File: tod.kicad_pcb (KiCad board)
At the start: 2 copper layers, 72 x 57 mm, 67 parts, among them J1 Conn_01x04, J2 Conn_01x03, J3 Conn_01x04, J4 Conn_01x03, Q1 BC856B, Q2 BC817, Q3 BC856B, Q4 BC817, Q5 BC856, Q6 BC817, Q7 BC856, Q8 BC817, U1 PC817, U2 PC817, U3 PC817, U4 PC817

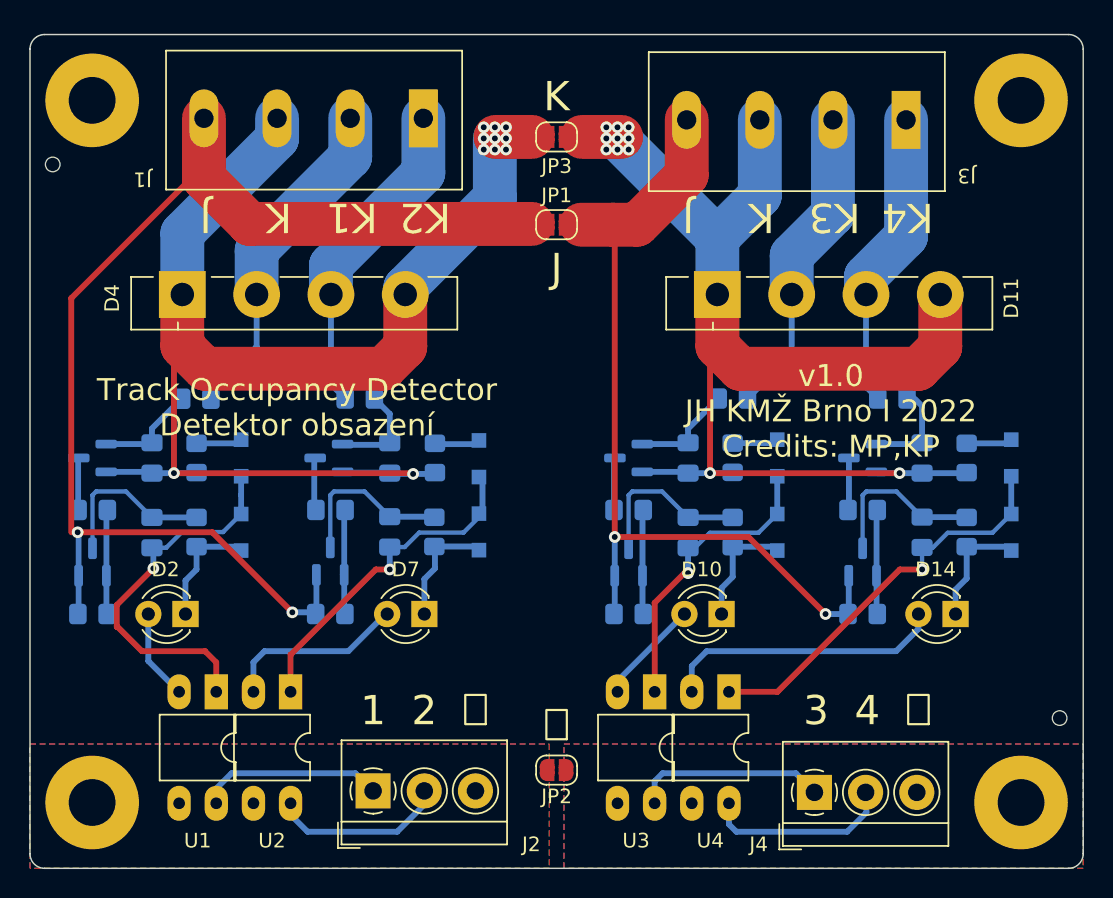
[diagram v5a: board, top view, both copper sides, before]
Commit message: Resolve DRC issues.
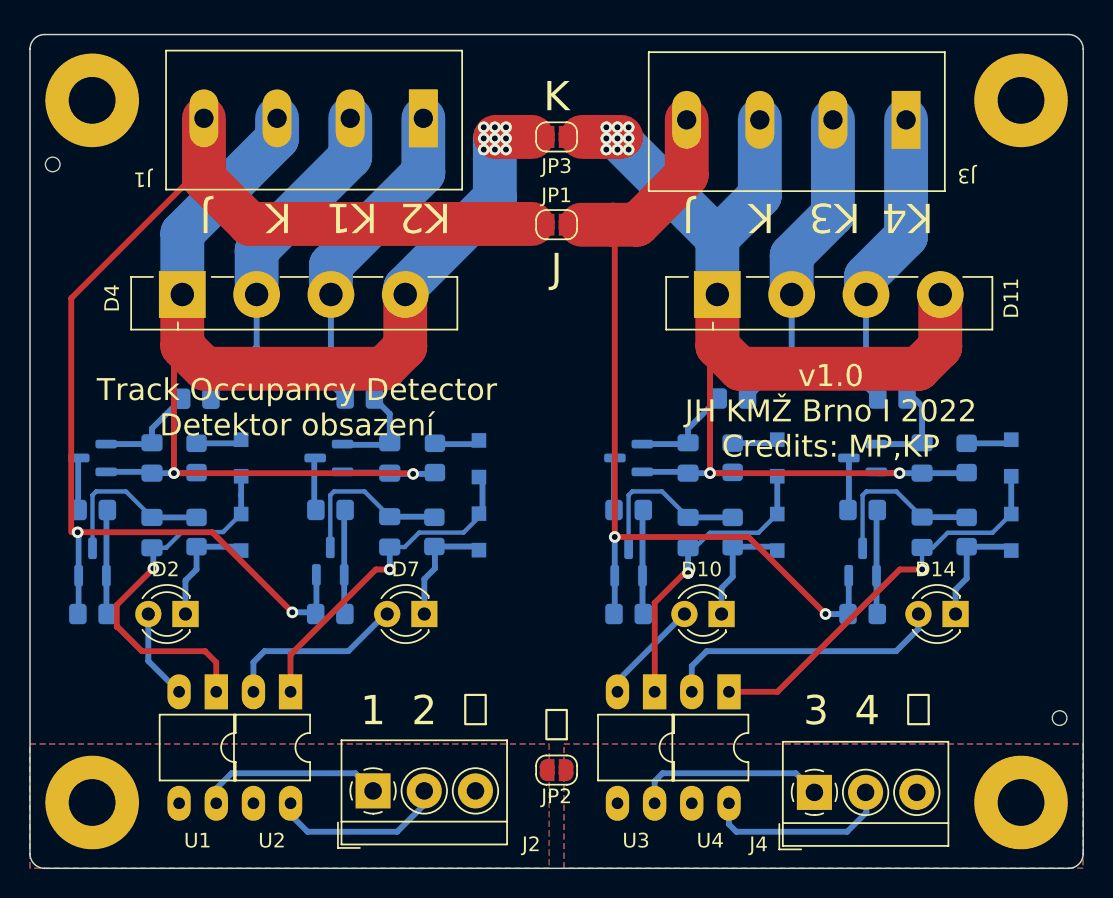
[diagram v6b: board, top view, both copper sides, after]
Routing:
- net /K1: track 93.5 -> 92.0 mm
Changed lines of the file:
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@@
   (segment (start 122.8405 92.9855) (end 122.862 92.964) (width 0.4) (layer "F.Cu") (net 1))
   (segment (start 138.654 84.358) (end 137.16 85.852) (width 3) (layer "F.Cu") (net 1))
-  (segment (start 122.936 81.25) (end 123.414 80.772) (width 0.4) (layer "F.Cu") (net 1))
   (segment (start 124.968 85.852) (end 123.414 84.298) (width 3) (layer "F.Cu") (net 1))
   (segment (start 122.8405 92.9855) (end 139.1395 92.9855) (width 0.4) (layer "F.Cu") (net 1))
-  (segment (start 122.8405 81.3455) (end 123.414 80.772) (width 0.4) (layer "F.Cu") (net 1))
   (segment (start 144.82 70) (end 147.32 70) (width 3) (layer "F.Cu") (net 1))
   (segment (start 122.8405 84.8715) (end 123.414 84.298) (width 0.4) (layer "F.Cu") (net 1))
@@
   (segment (start 137.434 95.9625) (end 140.6465 95.9625) (width 0.4) (layer "B.Cu") (net 7))
   (segment (start 133.53 98.0625) (end 133.53 94.488) (width 0.3) (layer "B.Cu") (net 7))
-  (segment (start 140.6465 95.9625) (end 140.684 96) (width 0.4) (layer "B.Cu") (net 7))
   (segment (start 175.23 80.772) (end 175.23 84.358) (width 3) (layer "F.Cu") (net 8))
   (segment (start 175.23 84.358) (end 173.736 85.852) (width 3) (layer "F.Cu") (net 8))
@@
   (segment (start 173.985 92.9855) (end 176.9955 92.9855) (width 0.4) (layer "B.Cu") (net 8))
   (segment (start 173.985 92.9855) (end 170.946 92.9855) (width 0.4) (layer "B.Cu") (net 8))
-  (segment (start 173.8975 92.898) (end 173.985 92.9855) (width 0.4) (layer "B.Cu") (net 8))
   (segment (start 157.988 89.948) (end 160.052 87.884) (width 0.4) (layer "B.Cu") (net 9))
   (segment (start 154.8615 90.998) (end 157.9005 90.998) (width 0.4) (layer "B.Cu") (net 9))
@@
   (segment (start 130.934 102.5) (end 132.414 102.5) (width 0.4) (layer "B.Cu") (net 31))
   (segment (start 116.324 102.582) (end 116.29 102.616) (width 0.4) (layer "B.Cu") (net 31))
-  (segment (start 132.484 102.7) (end 132.434 102.75) (width 0.4) (layer "B.Cu") (net 31))
-  (segment (start 132.414 102.5) (end 132.53 102.616) (width 0.4) (layer "B.Cu") (net 31))
-  (segment (start 132.58 102.566) (end 132.53 102.616) (width 0.4) (layer "B.Cu") (net 31))
   (segment (start 116.324 99.9975) (end 116.324 97.094) (width 0.4) (layer "B.Cu") (net 31))
   (segment (start 125.735 115.555) (end 125.735 114.549) (width 0.4) (layer "B.Cu") (net 32))
@@
   (segment (start 134.48 99.9375) (end 134.48 102.566) (width 0.4) (layer "B.Cu") (net 41))
   (segment (start 134.48 95.566) (end 134.546 95.5) (width 0.4) (layer "B.Cu") (net 41))
-  (segment (start 134.434 99.8875) (end 134.384 99.9375) (width 0.4) (layer "B.Cu") (net 41))
   (segment (start 134.384 102.7) (end 134.434 102.75) (width 0.4) (layer "B.Cu") (net 41))
   (segment (start 134.48 102.566) (end 134.53 102.616) (width 0.4) (layer "B.Cu") (net 41))

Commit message: Minor silkscreen tweaks.
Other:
- board text added: "v1.0 JH KMŽ Brno I 2022"
- board text removed: "v1.0 JH KMŽ Brno I 2022 Credits: MP,KP"
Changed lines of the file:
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@@
     (effects (font (size 2 2) (thickness 0.15)))
   )
-  (gr_text "v1.0\nJH KMŽ Brno I 2022\nCredits: MP,KP" (at 167.75 88.75) (layer "F.SilkS")
+  (gr_text "v1.0\nJH KMŽ Brno I 2022" (at 167.75 88.75) (layer "F.SilkS")
     (effects (font (size 1.5 1.5) (thickness 0.15)))
   )
@@
   (segment (start 172.212 105.156) (end 159.258 105.156) (width 0.4) (layer "B.Cu") (net 30))
   (segment (start 173.736 102.616) (end 173.736 103.632) (width 0.4) (layer "B.Cu") (net 30))
-  (segment (start 123.824 73.026) (end 123.824 69) (width 0.4) (layer "F.Cu") (net 31))
+  (segment (start 116.332 80.518) (end 116.332 96.954) (width 0.4) (layer "F.Cu") (net 31))
   (segment (start 125.462 97.028) (end 130.934 102.5) (width 0.4) (layer "F.Cu") (net 31))
-  (segment (start 115.824 97.028) (end 115.824 81.026) (width 0.4) (layer "F.Cu") (net 31))
+  (segment (start 116.332 96.954) (end 116.258 97.028) (width 0.4) (layer "F.Cu") (net 31))
   (segment (start 128.016 75.946) (end 147.32 75.946) (width 3) (layer "F.Cu") (net 31))
   (segment (start 124.892 72.822) (end 124.892 68.728) (width 3) (layer "F.Cu") (net 31))
+  (segment (start 123.824 73.026) (end 116.332 80.518) (width 0.4) (layer "F.Cu") (net 31))
   (segment (start 128.016 75.946) (end 124.892 72.822) (width 3) (layer "F.Cu") (net 31))
-  (segment (start 115.824 81.026) (end 123.824 73.026) (width 0.4) (layer "F.Cu") (net 31))
+  (segment (start 123.824 69) (end 123.824 73.026) (width 0.4) (layer "F.Cu") (net 31))
   (segment (start 116.258 97.028) (end 125.462 97.028) (width 0.4) (layer "F.Cu") (net 31))
   (via (at 116.258 97.028) (size 0.8) (drill 0.4) (layers "F.Cu" "B.Cu") (net 31))

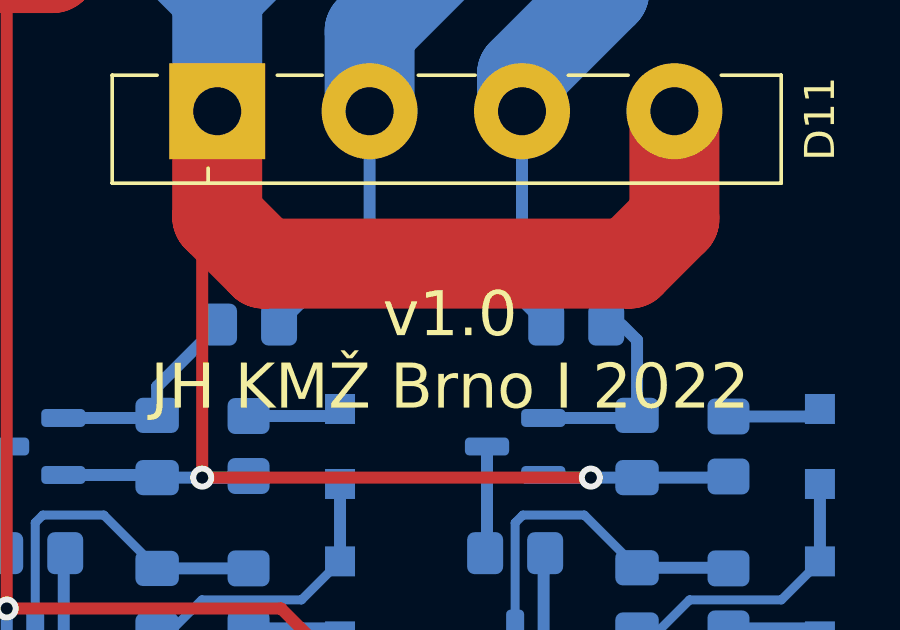
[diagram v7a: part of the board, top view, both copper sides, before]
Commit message: Add heat loss notice.
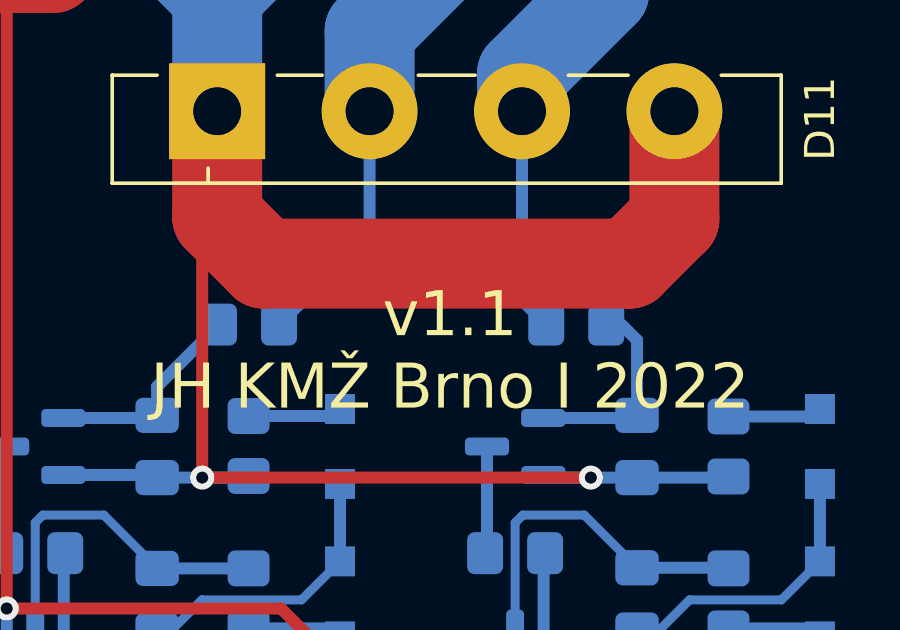
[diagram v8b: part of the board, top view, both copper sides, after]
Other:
- board text added: "v1.1 JH KMŽ Brno I 2022"
- board text removed: "v1.0 JH KMŽ Brno I 2022"
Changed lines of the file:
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@@
     (effects (font (size 2 2) (thickness 0.15)))
   )
-  (gr_text "v1.0\nJH KMŽ Brno I 2022" (at 167.75 88.75) (layer "F.SilkS")
+  (gr_text "v1.1\nJH KMŽ Brno I 2022" (at 167.75 88.75) (layer "F.SilkS")
     (effects (font (size 1.5 1.5) (thickness 0.15)))
   )
